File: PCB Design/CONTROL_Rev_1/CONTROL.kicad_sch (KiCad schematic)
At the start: 49 parts, among them J1 Conn_01x24_Pin, J2 Conn_01x24_Pin, J3 Micro_SD_Card, J4 USB_C_Receptacle_USB2.0_16P, SW1 SW_SPDT, U1 STM32F446RET6, U2 USBLC6-2SC6, Y1 16MHz, Y2 32.768KHz

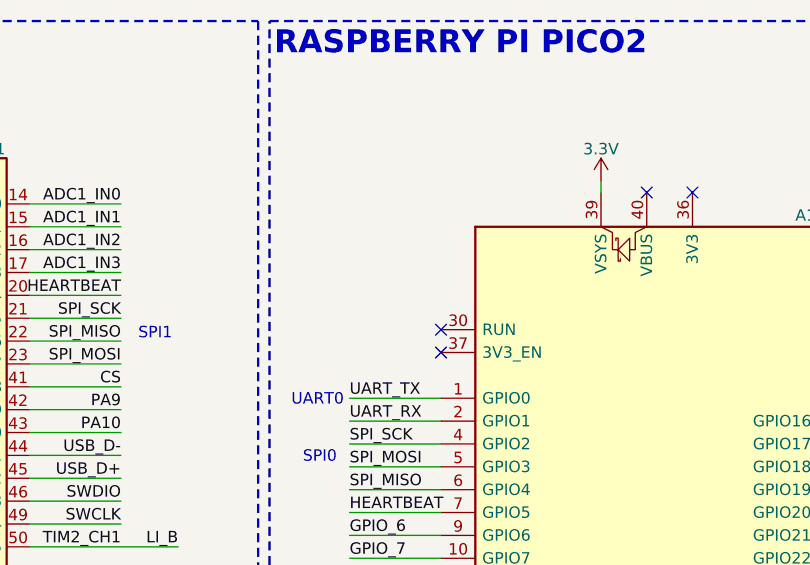
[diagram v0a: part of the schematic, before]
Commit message: fix(pico): connect power pins and add reset pull-up
- Connect VSYS (pin 39) to 3.3V rail via header
- Connect 3V3_EN (pin 37) to 3.3V to keep regulator enabled
- Add 10k pull-up resistor on RUN (pin 30) to 3.3V
- Add no-connect on 3V3 (pin 36) — Pico regulator output unused
- Add no-connect on VBUS (pin 40) — USB power not used
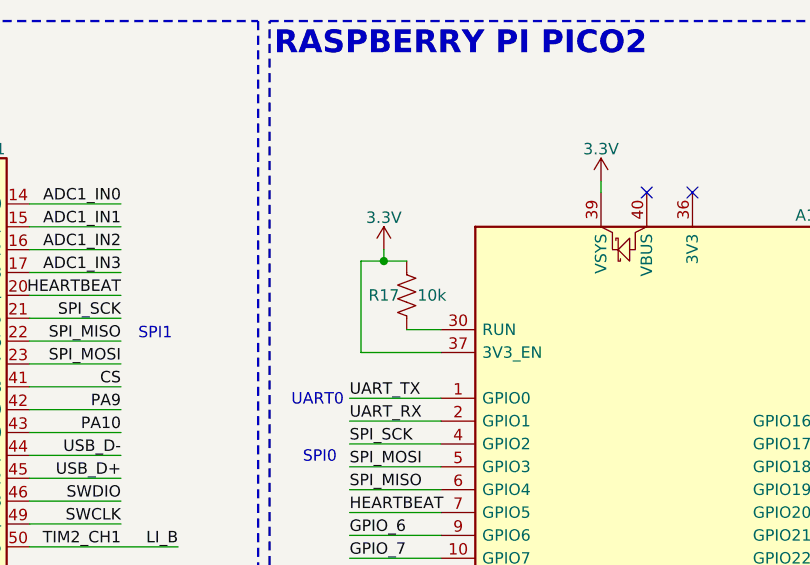
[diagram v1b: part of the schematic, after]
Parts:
- added R17: 10k, Resistor_SMD:R_0603_1608Metric, symbol Device:R_US
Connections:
- net 3.3V: now also A1.37 (3V3_EN), R17.2
- net at A1.30 (RUN): now also R17.1
- no-connect marks 7 -> 5
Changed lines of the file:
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@@
 	)
 	(junction
+		(at 125.73 40.64)
+		(diameter 0)
+		(color 0 0 0 0)
+	)
+	(junction
 		(at 115.57 176.53)
 		(diameter 0)
@@
 	)
 	(no_connect
-		(at 132.08 48.26)
-	)
-	(no_connect
-		(at 132.08 50.8)
-	)
-	(no_connect
 		(at 177.8 93.98)
 	)
@@
 	(wire
 		(pts
+			(xy 125.73 39.37) (xy 125.73 40.64)
+		)
+		(stroke
+			(width 0)
+			(type default)
+		)
+	)
+	(wire
+		(pts
+			(xy 123.19 40.64) (xy 123.19 50.8)
+		)
+		(stroke
+			(width 0)
+			(type default)
+		)
+	)
+	(wire
+		(pts
 			(xy 115.57 168.91) (xy 115.57 176.53)
 		)
@@
 	(wire
 		(pts
+			(xy 123.19 50.8) (xy 132.08 50.8)
+		)
+		(stroke
+			(width 0)
+			(type default)
+		)
+	)
+	(wire
+		(pts
 			(xy 177.8 86.36) (xy 185.42 86.36)
 		)
@@
 	(wire
 		(pts
+			(xy 125.73 40.64) (xy 128.27 40.64)
+		)
+		(stroke
+			(width 0)
+			(type default)
+		)
+	)
+	(wire
+		(pts
 			(xy 275.59 109.22) (xy 275.59 111.76)
 		)
@@
 	(wire
 		(pts
+			(xy 128.27 48.26) (xy 132.08 48.26)
+		)
+		(stroke
+			(width 0)
+			(type default)
+		)
+	)
+	(wire
+		(pts
 			(xy 63.5 26.67) (xy 66.04 26.67)
 		)
@@
 	(wire
 		(pts
+			(xy 125.73 40.64) (xy 123.19 40.64)
+		)
+		(stroke
+			(width 0)
+			(type default)
+		)
+	)
+	(wire
+		(pts
 			(xy 86.36 87.63) (xy 96.52 87.63)
 		)
@@
 	)
 	(symbol
+		(lib_id "power:VCC")
+		(at 125.73 39.37 0)
+		(unit 1)
+		(exclude_from_sim no)
+		(in_bom yes)
+		(on_board yes)
+		(dnp no)
+		(property "Reference" "#PWR027"
+			(at 125.73 43.18 0)
+			(effects
+				(font
+					(size 1.27 1.27)
+				)
+				(hide yes)
+			)
+		)
+		(property "Value" "3.3V"
+			(at 125.73 35.814 0)
+			(effects
+				(font
+					(size 1.27 1.27)
+				)
+			)
+		)
+		(property "Footprint" ""
+			(at 125.73 39.37 0)
+			(effects
+				(font
+					(size 1.27 1.27)
+				)
+				(hide yes)
+			)
+		)
+		(property "Datasheet" ""
+			(at 125.73 39.37 0)
+			(effects
+				(font
+					(size 1.27 1.27)
+				)
+				(hide yes)
+			)
+		)
+		(property "Description" "Power symbol creates a global label with name \"VCC\""
+			(at 125.73 39.37 0)
+			(effects
+				(font
+					(size 1.27 1.27)
+				)
+				(hide yes)
+			)
+		)
+		(pin "1"
+		)
+		(instances
+			(project "CONTROL"
+				(path "/0692d2c3-ddc7-44ef-a4e6-56d2a9ee62f1"
+					(reference "#PWR027")
+					(unit 1)
+				)
+			)
+		)
+	)
+	(symbol
 		(lib_id "power:GND")
 		(at 172.72 191.77 0)
@@
 					(unit 1)
 				)
+			)
+		)
+	)
+	(symbol
+		(lib_id "Device:R_US")
+		(at 128.27 44.45 180)
+		(unit 1)
+		(exclude_from_sim no)
+		(in_bom yes)
+		(on_board yes)
+		(dnp no)
+		(property "Reference" "R17"
+			(at 125.73 44.45 0)
+			(effects
+				(font
+					(size 1.27 1.27)
+				)
+			)
+		)
+		(property "Value" "10k"
+			(at 131.064 44.45 0)
+			(effects
+				(font
+					(size 1.27 1.27)
+				)
+			)
+		)
+		(property "Footprint" "Resistor_SMD:R_0603_1608Metric"
+			(at 127.254 44.196 90)
+			(effects
+				(font
+					(size 1.27 1.27)
+				)
+				(hide yes)
+			)
+		)
+		(property "Datasheet" "~"
+			(at 128.27 44.45 0)
+			(effects
+				(font
+					(size 1.27 1.27)
+				)
+				(hide yes)
+			)
+		)
+		(property "Description" "Resistor, US symbol"
+			(at 128.27 44.45 0)
+			(effects
+				(font
+					(size 1.27 1.27)
+				)
+				(hide yes)
+			)
+		)
+		(pin "2"
+		)
+		(pin "1"
+		)
+		(instances
+			(project "CONTROL"
+				(path "/0692d2c3-ddc7-44ef-a4e6-56d2a9ee62f1"
+					(reference "R17")
+					(unit 1)
+				)

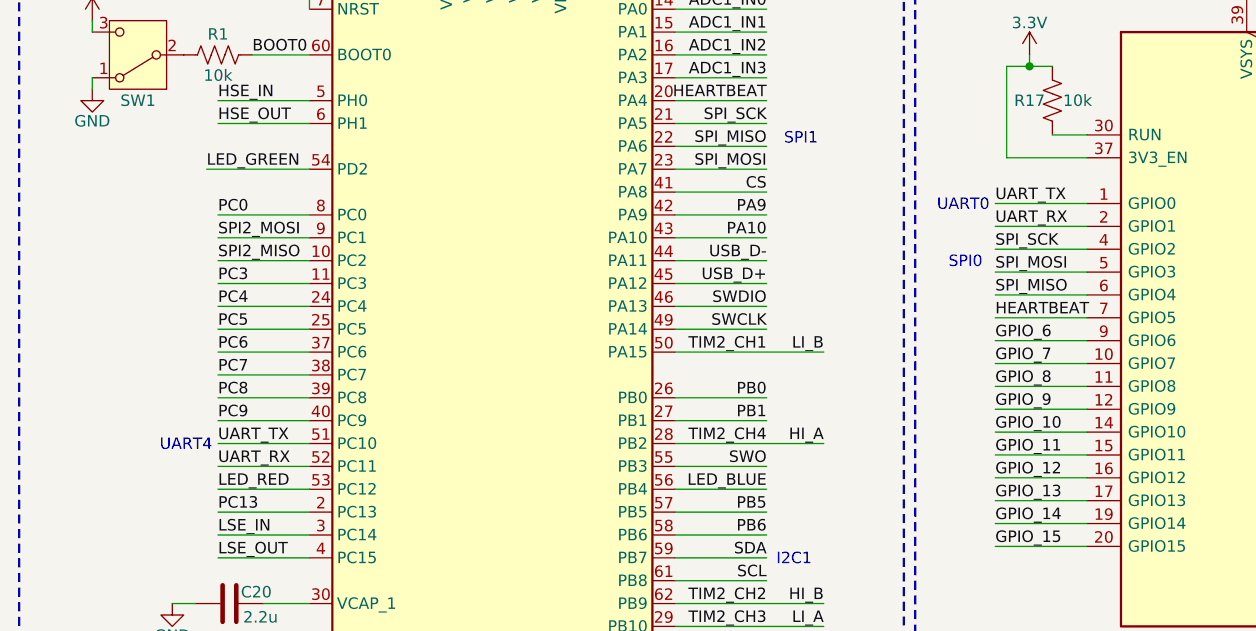
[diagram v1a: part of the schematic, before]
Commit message: fix(uart): correct inter-MCU UART cross-connection
- Swap UART net labels on Pico side to correctly cross TX/RX
- Pico GPIO4 (pin 6): UART_TX -> UART_RX (connects to STM32 PA9/USART1_TX)
- Pico GPIO5 (pin 7): UART_RX -> UART_TX (connects to STM32 PA10/USART1_RX)
- Both MCUs confirmed on 3.3V — no level shifting required
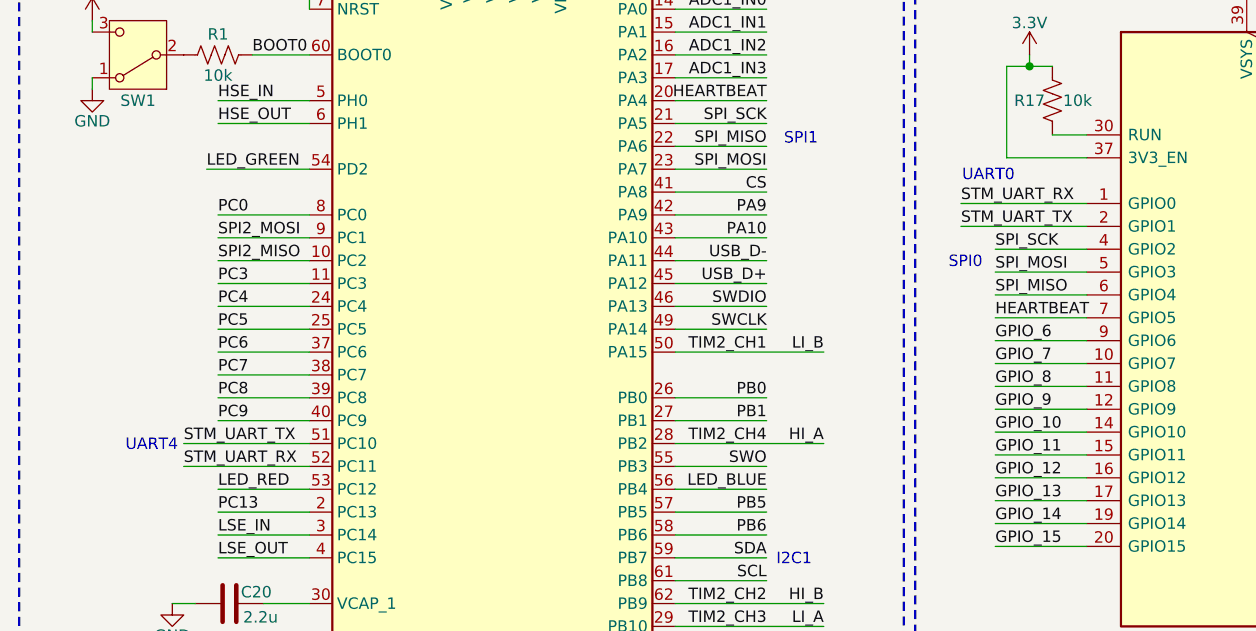
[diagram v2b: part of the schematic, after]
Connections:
- net UART_RX renamed STM_UART_RX
- net STM_UART_RX: now also A1.1 (GPIO0); no longer A1.2 (GPIO1)
- net UART_TX renamed STM_UART_TX
- net STM_UART_TX: now also A1.2 (GPIO1); no longer A1.1 (GPIO0)
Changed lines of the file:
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@@
 	(text "UART0"
 		(exclude_from_sim no)
-		(at 118.364 56.134 0)
+		(at 121.158 52.832 0)
 		(effects
 			(font
@@
 	(text "UART4"
 		(exclude_from_sim no)
-		(at 32.004 82.804 0)
+		(at 28.194 82.804 0)
 		(effects
 			(font
@@
 	(wire
 		(pts
-			(xy 121.92 58.42) (xy 132.08 58.42)
+			(xy 118.11 58.42) (xy 132.08 58.42)
 		)
 		(stroke
@@
 	(wire
 		(pts
-			(xy 35.56 85.09) (xy 45.72 85.09)
+			(xy 31.75 85.09) (xy 45.72 85.09)
 		)
 		(stroke
@@
 	(wire
 		(pts
-			(xy 121.92 55.88) (xy 132.08 55.88)
+			(xy 118.11 55.88) (xy 132.08 55.88)
 		)
 		(stroke
@@
 	(wire
 		(pts
-			(xy 35.56 82.55) (xy 45.72 82.55)
+			(xy 31.75 82.55) (xy 45.72 82.55)
 		)
 		(stroke
@@
 		)
 	)
-	(label "UART_RX"
-		(at 35.56 85.09 0)
+	(label "STM_UART_RX"
+		(at 31.75 85.09 0)
 		(effects
 			(font
@@
 		)
 	)
-	(label "UART_RX"
-		(at 121.92 58.42 0)
+	(label "STM_UART_TX"
+		(at 118.11 58.42 0)
 		(effects
 			(font
@@
 		)
 	)
-	(label "UART_TX"
-		(at 121.92 55.88 0)
+	(label "STM_UART_RX"
+		(at 118.11 55.88 0)
 		(effects
 			(font
@@
 		)
 	)
-	(label "UART_TX"
-		(at 35.56 82.55 0)
+	(label "STM_UART_TX"
+		(at 31.75 82.55 0)
 		(effects
 			(font

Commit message: CONTROL - Added 3D Models for Export
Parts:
- D2: footprint LED_SMD:LED_RGB_PLCC-6 -> CONTROL:LED_RGB_PLCC-6
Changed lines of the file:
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@@
 			)
 		)
-		(property "Footprint" "LED_SMD:LED_RGB_PLCC-6"
+		(property "Footprint" "CONTROL:LED_RGB_PLCC-6"
 			(at 208.28 86.36 0)
 			(effects

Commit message: Updated
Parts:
- removed J1, J2: Conn_01x24_Pin, Connector_PinHeader_2.54mm:PinHeader_1x24_P2.54mm_Vertical, symbol Connector:Conn_01x24_Pin
- added J1, J2, J3, J4: Conn_02x25_Odd_Even, CONTROL:HIROSE_DF40C-50DP-0.4V_51_, symbol Connector_Generic:Conn_02x25_Odd_Even
- renumbered J3 to J5, J4 to J6
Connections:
- net 3.3V: now also J1.3 (Pin_3), J1.4 (Pin_4), J1.5 (Pin_5), J1.6 (Pin_6), J1.7 (Pin_7), J1.8 (Pin_8), J3.3 (Pin_3), J3.4 (Pin_4), J3.5 (Pin_5), J3.6 (Pin_6), J3.7 (Pin_7), J3.8 (Pin_8)
- net ADC1_IN0: now also J1.31 (Pin_31), J1.32 (Pin_32), J3.31 (Pin_31), J3.32 (Pin_32)
- net ADC1_IN1: now also J1.33 (Pin_33), J1.34 (Pin_34), J3.33 (Pin_33), J3.34 (Pin_34)
- net ADC1_IN2: now also J1.35 (Pin_35), J1.36 (Pin_36), J3.35 (Pin_35), J3.36 (Pin_36)
- net ADC1_IN3: now also J1.37 (Pin_37), J1.38 (Pin_38), J3.37 (Pin_37), J3.38 (Pin_38)
- net GND: now also J1.1 (Pin_1), J1.10 (Pin_10), J1.11 (Pin_11), J1.12 (Pin_12), J1.2 (Pin_2), J1.49 (Pin_49), J1.50 (Pin_50), J1.9 (Pin_9), J2.49 (Pin_49), J2.50 (Pin_50), J3.1 (Pin_1), J3.10 (Pin_10), J3.11 (Pin_11), J3.12 (Pin_12), J3.2 (Pin_2), J3.49 (Pin_49), J3.50 (Pin_50), J3.9 (Pin_9), J4.49 (Pin_49), J4.50 (Pin_50)
- net GPIO_10: now also J1.21 (Pin_21), J1.22 (Pin_22), J3.21 (Pin_21), J3.22 (Pin_22)
- net GPIO_11: now also J1.23 (Pin_23), J1.24 (Pin_24), J3.23 (Pin_23), J3.24 (Pin_24)
- net GPIO_12: now also J1.25 (Pin_25), J1.26 (Pin_26), J3.25 (Pin_25), J3.26 (Pin_26)
- net GPIO_13: now also J1.27 (Pin_27), J1.28 (Pin_28), J3.27 (Pin_27), J3.28 (Pin_28)
- net GPIO_14: now also J1.29 (Pin_29), J1.30 (Pin_30), J3.29 (Pin_29), J3.30 (Pin_30)
- net GPIO_16: now also J2.15 (Pin_15), J2.16 (Pin_16), J4.15 (Pin_15), J4.16 (Pin_16)
- net GPIO_17: now also J2.13 (Pin_13), J2.14 (Pin_14), J4.13 (Pin_13), J4.14 (Pin_14)
- net GPIO_26: now also J2.11 (Pin_11), J2.12 (Pin_12), J4.11 (Pin_11), J4.12 (Pin_12)
- net GPIO_27: now also J2.10 (Pin_10), J2.9 (Pin_9), J4.10 (Pin_10), J4.9 (Pin_9)
- net GPIO_28: now also J2.7 (Pin_7), J2.8 (Pin_8), J4.7 (Pin_7), J4.8 (Pin_8)
- net GPIO_6: now also J1.13 (Pin_13), J1.14 (Pin_14), J3.13 (Pin_13), J3.14 (Pin_14)
- net GPIO_7: now also J1.15 (Pin_15), J1.16 (Pin_16), J3.15 (Pin_15), J3.16 (Pin_16)
- net GPIO_8: now also J1.17 (Pin_17), J1.18 (Pin_18), J3.17 (Pin_17), J3.18 (Pin_18)
- net GPIO_9: now also J1.19 (Pin_19), J1.20 (Pin_20), J3.19 (Pin_19), J3.20 (Pin_20)
- net HI_A: now also J1.45 (Pin_45), J1.46 (Pin_46), J3.45 (Pin_45), J3.46 (Pin_46)
- net HI_B: now also J2.45 (Pin_45), J2.46 (Pin_46), J4.45 (Pin_45), J4.46 (Pin_46)
- net LI_A: now also J1.47 (Pin_47), J1.48 (Pin_48), J3.47 (Pin_47), J3.48 (Pin_48)
- net LI_B: now also J2.47 (Pin_47), J2.48 (Pin_48), J4.47 (Pin_47), J4.48 (Pin_48)
- net PA10: now also J2.35 (Pin_35), J2.36 (Pin_36), J4.35 (Pin_35), J4.36 (Pin_36)
- net PA9: now also J2.33 (Pin_33), J2.34 (Pin_34), J4.33 (Pin_33), J4.34 (Pin_34)
- net PB0: now also J1.41 (Pin_41), J1.42 (Pin_42), J3.41 (Pin_41), J3.42 (Pin_42)
- net PB1: now also J1.43 (Pin_43), J1.44 (Pin_44), J3.43 (Pin_43), J3.44 (Pin_44)
- net PB12: now also J2.19 (Pin_19), J2.20 (Pin_20), J4.19 (Pin_19), J4.20 (Pin_20)
- net PB14: now also J2.21 (Pin_21), J2.22 (Pin_22), J4.21 (Pin_21), J4.22 (Pin_22)
- net PB15: now also J2.23 (Pin_23), J2.24 (Pin_24), J4.23 (Pin_23), J4.24 (Pin_24)
- net PB5: now also J2.43 (Pin_43), J2.44 (Pin_44), J4.43 (Pin_43), J4.44 (Pin_44)
- net PB6: now also J2.41 (Pin_41), J2.42 (Pin_42), J4.41 (Pin_41), J4.42 (Pin_42)
- net PC0: now also J2.3 (Pin_3), J2.4 (Pin_4), J4.3 (Pin_3), J4.4 (Pin_4)
- net PC13: now also J2.5 (Pin_5), J2.6 (Pin_6), J4.5 (Pin_5), J4.6 (Pin_6)
- net PC3: now also J2.1 (Pin_1), J2.2 (Pin_2), J4.1 (Pin_1), J4.2 (Pin_2)
- net PC4: now also J2.17 (Pin_17), J2.18 (Pin_18), J4.17 (Pin_17), J4.18 (Pin_18)
- net PC5: now also J1.39 (Pin_39), J1.40 (Pin_40), J3.39 (Pin_39), J3.40 (Pin_40)
- net PC6: now also J2.25 (Pin_25), J2.26 (Pin_26), J4.25 (Pin_25), J4.26 (Pin_26)
- net PC7: now also J2.27 (Pin_27), J2.28 (Pin_28), J4.27 (Pin_27), J4.28 (Pin_28)
- net PC8: now also J2.29 (Pin_29), J2.30 (Pin_30), J4.29 (Pin_29), J4.30 (Pin_30)
- net PC9: now also J2.31 (Pin_31), J2.32 (Pin_32), J4.31 (Pin_31), J4.32 (Pin_32)
- net SCL: now also J2.37 (Pin_37), J2.38 (Pin_38), J4.37 (Pin_37), J4.38 (Pin_38)
- net SDA: now also J2.39 (Pin_39), J2.40 (Pin_40), J4.39 (Pin_39), J4.40 (Pin_40)
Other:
- moved on the sheet: A1, C10, C17, C18, C19, C20, D1, D2, D3, R1, R10, R13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

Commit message: Revert "Updated"
This reverts commit 89be44ed720659141c8ee702c54a520a60db740f.
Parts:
- removed J1, J2, J3, J4: Conn_02x25_Odd_Even, CONTROL:HIROSE_DF40C-50DP-0.4V_51_, symbol Connector_Generic:Conn_02x25_Odd_Even
- added J1, J2: Conn_01x24_Pin, Connector_PinHeader_2.54mm:PinHeader_1x24_P2.54mm_Vertical, symbol Connector:Conn_01x24_Pin
- renumbered J5 to J3, J6 to J4
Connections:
- net 12V: now also J1.3 (Pin_3)
- net 3.3V: now also J1.1 (Pin_1)
- net ADC1_IN0: now also J1.16 (Pin_16)
- net ADC1_IN1: now also J1.17 (Pin_17)
- net ADC1_IN2: now also J1.18 (Pin_18)
- net ADC1_IN3: now also J1.19 (Pin_19)
- net GND: now also J1.2 (Pin_2), J1.4 (Pin_4), J1.6 (Pin_6)
- net GPIO_10: now also J1.11 (Pin_11)
- net GPIO_11: now also J1.12 (Pin_12)
- net GPIO_12: now also J1.13 (Pin_13)
- net GPIO_13: now also J1.14 (Pin_14)
- net GPIO_14: now also J1.15 (Pin_15)
- net GPIO_16: now also J2.8 (Pin_8)
- net GPIO_17: now also J2.7 (Pin_7)
- net GPIO_26: now also J2.6 (Pin_6)
- net GPIO_27: now also J2.5 (Pin_5)
- net GPIO_28: now also J2.4 (Pin_4)
- net GPIO_6: now also J1.7 (Pin_7)
- net GPIO_7: now also J1.8 (Pin_8)
- net GPIO_8: now also J1.9 (Pin_9)
- net GPIO_9: now also J1.10 (Pin_10)
- net HI_A: now also J1.23 (Pin_23)
- net HI_B: now also J2.23 (Pin_23)
- net LI_A: now also J1.24 (Pin_24)
- net LI_B: now also J2.24 (Pin_24)
- net PA10: now also J2.18 (Pin_18)
- net PA9: now also J2.17 (Pin_17)
- net PB0: now also J1.21 (Pin_21)
- net PB1: now also J1.22 (Pin_22)
- net PB12: now also J2.10 (Pin_10)
- net PB14: now also J2.11 (Pin_11)
- net PB15: now also J2.12 (Pin_12)
- net PB5: now also J2.22 (Pin_22)
- net PB6: now also J2.21 (Pin_21)
- net PC0: now also J2.2 (Pin_2)
- net PC13: now also J2.3 (Pin_3)
- net PC3: now also J2.1 (Pin_1)
- net PC4: now also J2.9 (Pin_9)
- net PC5: now also J1.20 (Pin_20)
- net PC6: now also J2.13 (Pin_13)
- net PC7: now also J2.14 (Pin_14)
- net PC8: now also J2.15 (Pin_15)
- net PC9: now also J2.16 (Pin_16)
- net SCL: now also J2.19 (Pin_19)
- net SDA: now also J2.20 (Pin_20)
- net V_Piezo: now also J1.5 (Pin_5)
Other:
- moved on the sheet: A1, C10, C17, C18, C19, C20, D1, D2, D3, R1, R10, R13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
